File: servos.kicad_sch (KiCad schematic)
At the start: 34 parts, among them J10 Conn_01x03_Male, J18 Conn_01x03_Male, J19 Conn_01x03_Male, J5 Conn_01x03_Male, J6 Conn_01x03_Male, J7 Conn_01x03_Male, J8 Conn_01x03_Male, J9 Conn_01x03_Male, Q5 DMP2040USD, Q6 DMP2040USD, Q8 Q_NMOS_DGS, Q9 Q_NMOS_DGS

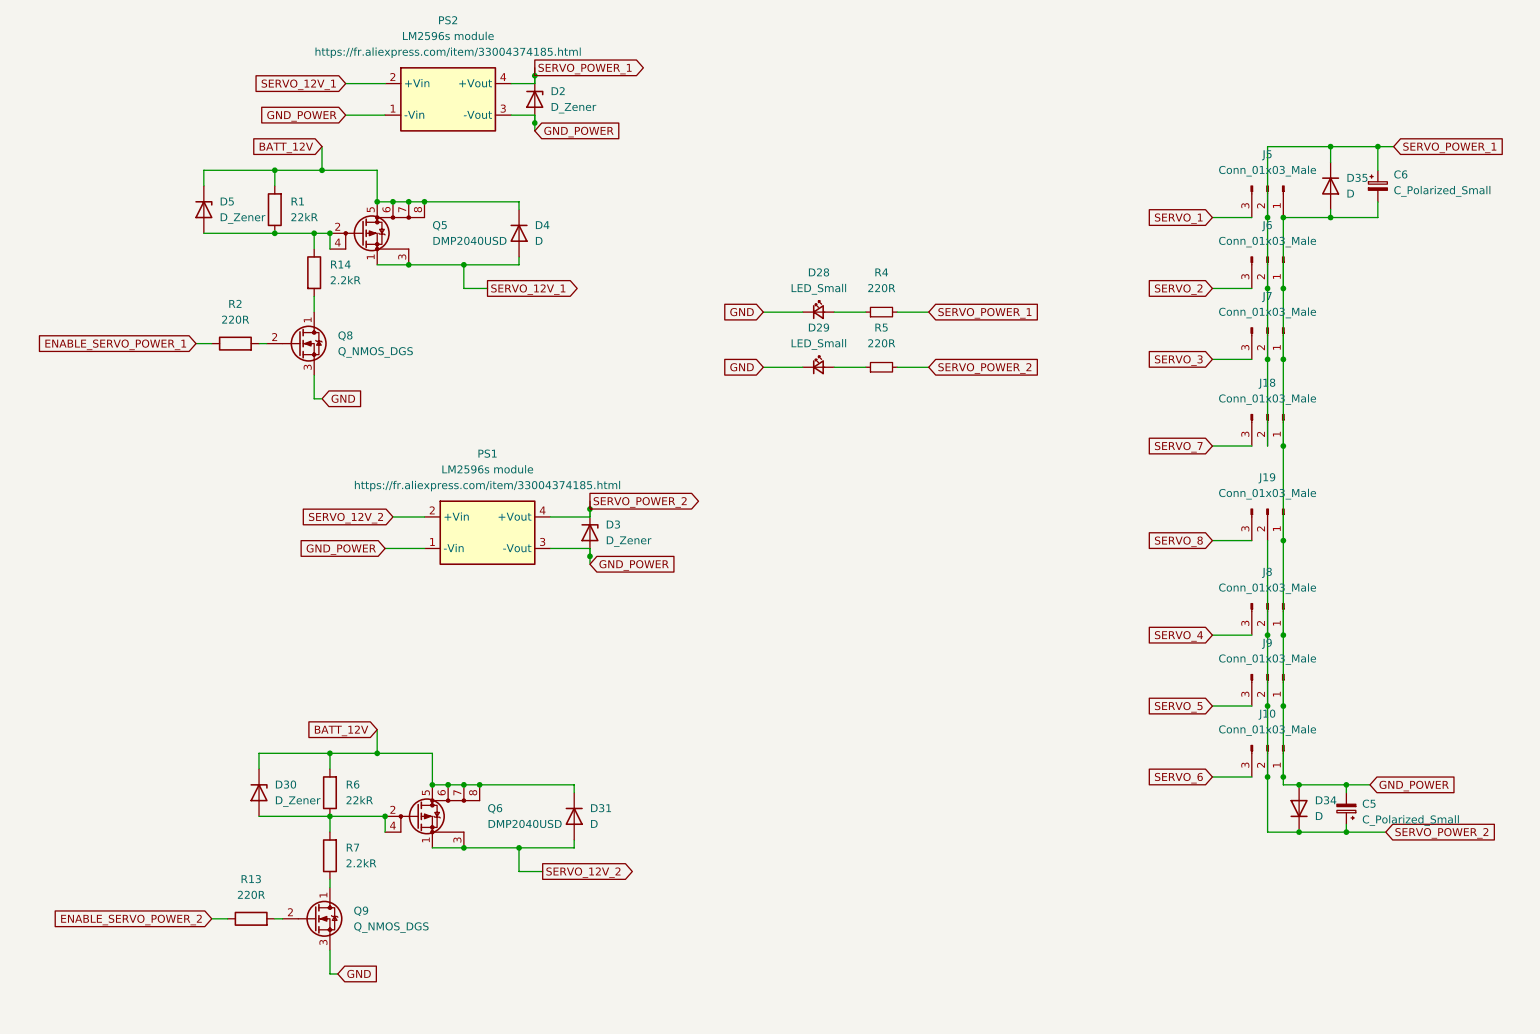
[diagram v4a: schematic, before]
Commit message: fix driving servo power (NMOS on GND) + fix 12V connector position
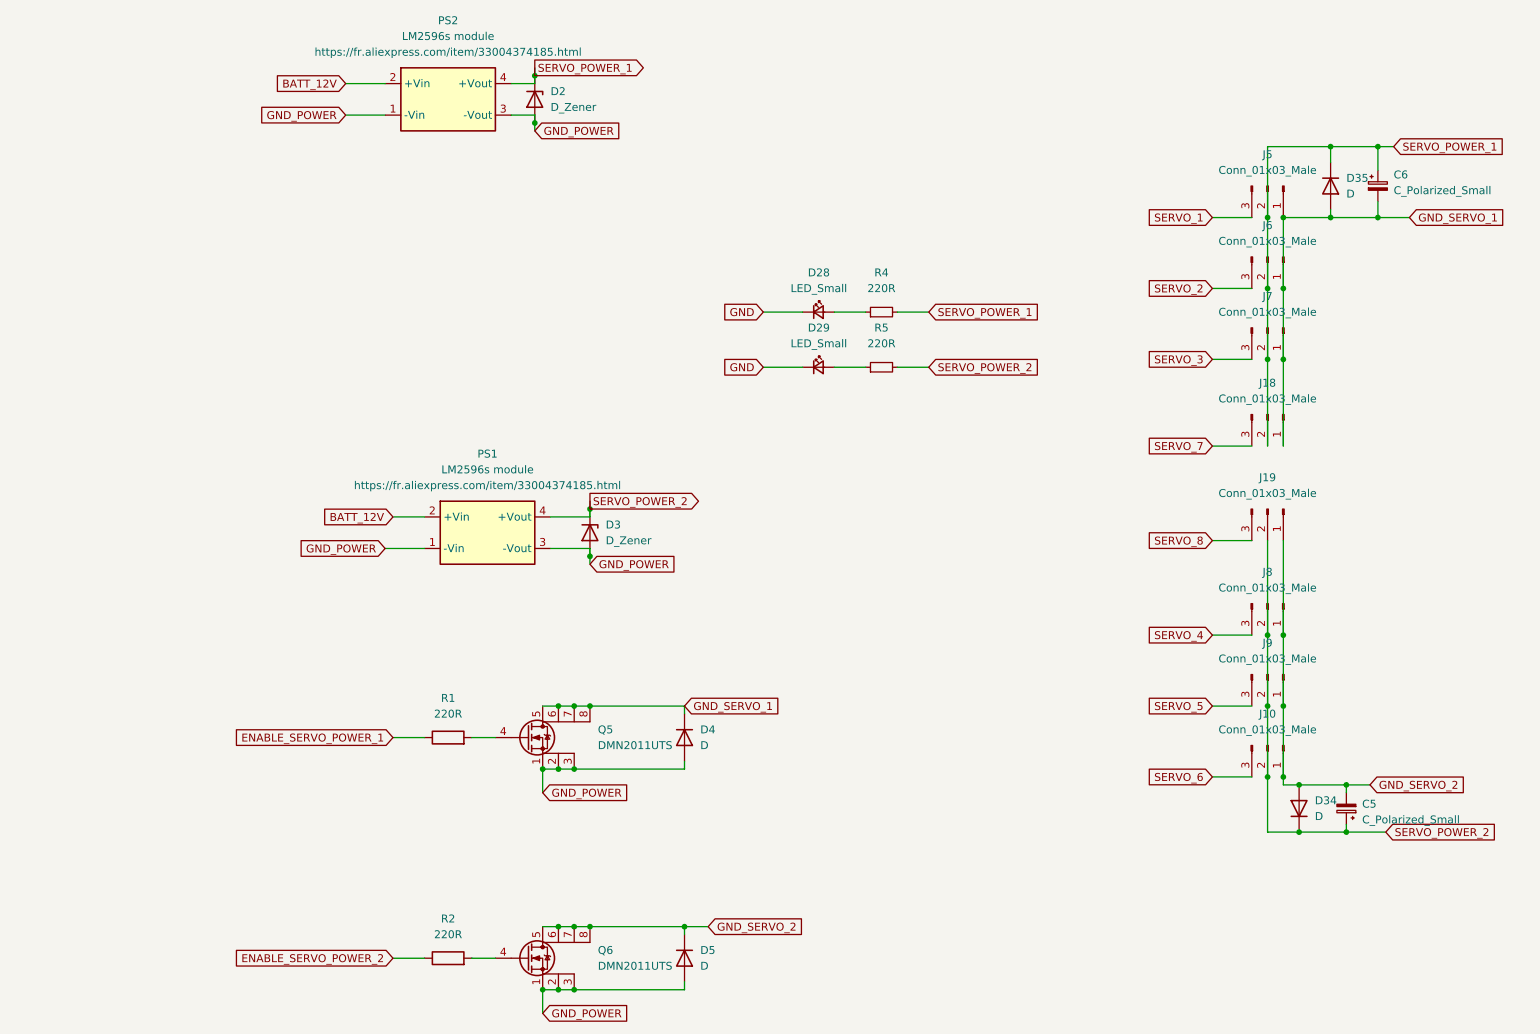
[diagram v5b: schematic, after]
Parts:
- removed D30, D5: D_Zener, Diode_SMD:D_1206_3216Metric, symbol Device:D_Zener
- removed D31: D, Diode_SMD:D_1206_3216Metric, symbol Device:D
- removed Q5, Q6: DMP2040USD, Package_SO:SO-8_3.9x4.9mm_P1.27mm, symbol New_Library_Victor:DMP2040USD
- removed Q8, Q9: Q_NMOS_DGS, symbol Device:Q_NMOS_DGS
- removed R13: 220R, Resistor_SMD:R_0603_1608Metric, symbol Device:R
- removed R14, R7: 2.2kR, Resistor_SMD:R_0603_1608Metric, symbol Device:R
- removed R6: 22kR, Resistor_SMD:R_0603_1608Metric, symbol Device:R
- added D5: D, Diode_SMD:D_1206_3216Metric, symbol Device:D
- added Q5, Q6: DMN2011UTS, Package_SO:TSSOP-8_4.4x3mm_P0.65mm, symbol New_Library_Victor:DMN2011UTS
- R1: value 22kR -> 220R
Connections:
- net SERVO_12V_2 is gone; now on net BATT_12V: PS1.2 (+Vin)
- net BATT_12V: now also PS2.2 (+Vin); no longer D4.1 (K), R1.2
- net ENABLE_SERVO_POWER_1: now also R1.1; no longer R2.1
- net ENABLE_SERVO_POWER_2: now also R2.1
- net GND_POWER: now also D4.2 (A), D5.2 (A), Q5.1 (S), Q5.2 (S), Q5.3 (S), Q6.1 (S), Q6.2 (S), Q6.3 (S); no longer C5.2, C6.2, D34.2 (A), D35.2 (A), J10.1 (Pin_1), J18.1 (Pin_1), J19.1 (Pin_1), J5.1 (Pin_1), J6.1 (Pin_1), J7.1 (Pin_1), J8.1 (Pin_1), J9.1 (Pin_1)
- net at R2.2: now also Q6.4 (G)
- removed net SERVO_12V_1: D4.2 (A), PS2.2 (+Vin)
- new net: Q5.4 (G), R1.2
- new net GND_SERVO_1: C6.2, D35.2 (A), D4.1 (K), J18.1 (Pin_1), J5.1 (Pin_1), J6.1 (Pin_1), J7.1 (Pin_1), Q5.5 (D), Q5.6 (D), Q5.7 (D), Q5.8 (D)
- new net GND_SERVO_2: C5.2, D34.2 (A), D5.1 (K), J10.1 (Pin_1), J19.1 (Pin_1), J8.1 (Pin_1), J9.1 (Pin_1), Q6.5 (D), Q6.6 (D), Q6.7 (D), Q6.8 (D)

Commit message: add AX12 connector + LED strip connector + libraries todo : add 12V connectors, change stepper connectors
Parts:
- J10, J18, J19, J5, J6, J7, J8, J9: footprint Connector_PinSocket_2.54mm:PinSocket_1x03_P2.54mm_Vertical -> Connector_PinHeader_2.54mm:PinHeader_1x03_P2.54mm_Vertical
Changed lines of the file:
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@@
     (property "Reference" "J7" (id 0) (at 210.82 69.85 90))
     (property "Value" "Conn_01x03_Male" (id 1) (at 210.82 72.39 90))
-    (property "Footprint" "Connector_PinSocket_2.54mm:PinSocket_1x03_P2.54mm_Vertical" (id 2) (at 210.82 74.93 0)
+    (property "Footprint" "Connector_PinHeader_2.54mm:PinHeader_1x03_P2.54mm_Vertical" (id 2) (at 210.82 74.93 0)
       (effects (font (size 1.27 1.27)) hide)
     )
@@
     (property "Reference" "J19" (id 0) (at 210.82 99.06 90))
     (property "Value" "Conn_01x03_Male" (id 1) (at 210.82 101.6 90))
-    (property "Footprint" "Connector_PinSocket_2.54mm:PinSocket_1x03_P2.54mm_Vertical" (id 2) (at 210.82 104.14 0)
+    (property "Footprint" "Connector_PinHeader_2.54mm:PinHeader_1x03_P2.54mm_Vertical" (id 2) (at 210.82 104.14 0)
       (effects (font (size 1.27 1.27)) hide)
     )
@@
     (property "Reference" "J5" (id 0) (at 210.82 46.99 90))
     (property "Value" "Conn_01x03_Male" (id 1) (at 210.82 49.53 90))
-    (property "Footprint" "Connector_PinSocket_2.54mm:PinSocket_1x03_P2.54mm_Vertical" (id 2) (at 210.82 52.07 0)
+    (property "Footprint" "Connector_PinHeader_2.54mm:PinHeader_1x03_P2.54mm_Vertical" (id 2) (at 210.82 52.07 0)
       (effects (font (size 1.27 1.27)) hide)
     )
@@
     (property "Reference" "J6" (id 0) (at 210.82 58.42 90))
     (property "Value" "Conn_01x03_Male" (id 1) (at 210.82 60.96 90))
-    (property "Footprint" "Connector_PinSocket_2.54mm:PinSocket_1x03_P2.54mm_Vertical" (id 2) (at 210.82 63.5 0)
+    (property "Footprint" "Connector_PinHeader_2.54mm:PinHeader_1x03_P2.54mm_Vertical" (id 2) (at 210.82 63.5 0)
       (effects (font (size 1.27 1.27)) hide)
     )
@@
     (property "Reference" "J10" (id 0) (at 210.82 137.16 90))
     (property "Value" "Conn_01x03_Male" (id 1) (at 210.82 139.7 90))
-    (property "Footprint" "Connector_PinSocket_2.54mm:PinSocket_1x03_P2.54mm_Vertical" (id 2) (at 210.82 142.24 0)
+    (property "Footprint" "Connector_PinHeader_2.54mm:PinHeader_1x03_P2.54mm_Vertical" (id 2) (at 210.82 142.24 0)
       (effects (font (size 1.27 1.27)) hide)
     )
@@
     (property "Reference" "J18" (id 0) (at 210.82 83.82 90))
     (property "Value" "Conn_01x03_Male" (id 1) (at 210.82 86.36 90))
-    (property "Footprint" "Connector_PinSocket_2.54mm:PinSocket_1x03_P2.54mm_Vertical" (id 2) (at 210.82 88.9 0)
+    (property "Footprint" "Connector_PinHeader_2.54mm:PinHeader_1x03_P2.54mm_Vertical" (id 2) (at 210.82 88.9 0)
       (effects (font (size 1.27 1.27)) hide)
     )
@@
     (property "Reference" "J9" (id 0) (at 210.82 125.73 90))
     (property "Value" "Conn_01x03_Male" (id 1) (at 210.82 128.27 90))
-    (property "Footprint" "Connector_PinSocket_2.54mm:PinSocket_1x03_P2.54mm_Vertical" (id 2) (at 210.82 130.81 0)
+    (property "Footprint" "Connector_PinHeader_2.54mm:PinHeader_1x03_P2.54mm_Vertical" (id 2) (at 210.82 130.81 0)
       (effects (font (size 1.27 1.27)) hide)
     )
@@
     (property "Reference" "J8" (id 0) (at 210.82 114.3 90))
     (property "Value" "Conn_01x03_Male" (id 1) (at 210.82 116.84 90))
-    (property "Footprint" "Connector_PinSocket_2.54mm:PinSocket_1x03_P2.54mm_Vertical" (id 2) (at 210.82 119.38 0)
-      (effects (font (size 1.27 1.27)) hide)
-    )
+    (property "Footprint" "Connector_PinHeader_2.54mm:PinHeader_1x03_P2.54mm_Vertical" (id 2) (at 210.82 119.38 0)
+      (effects (font (size 1.27 1.27)) hide)
+    )

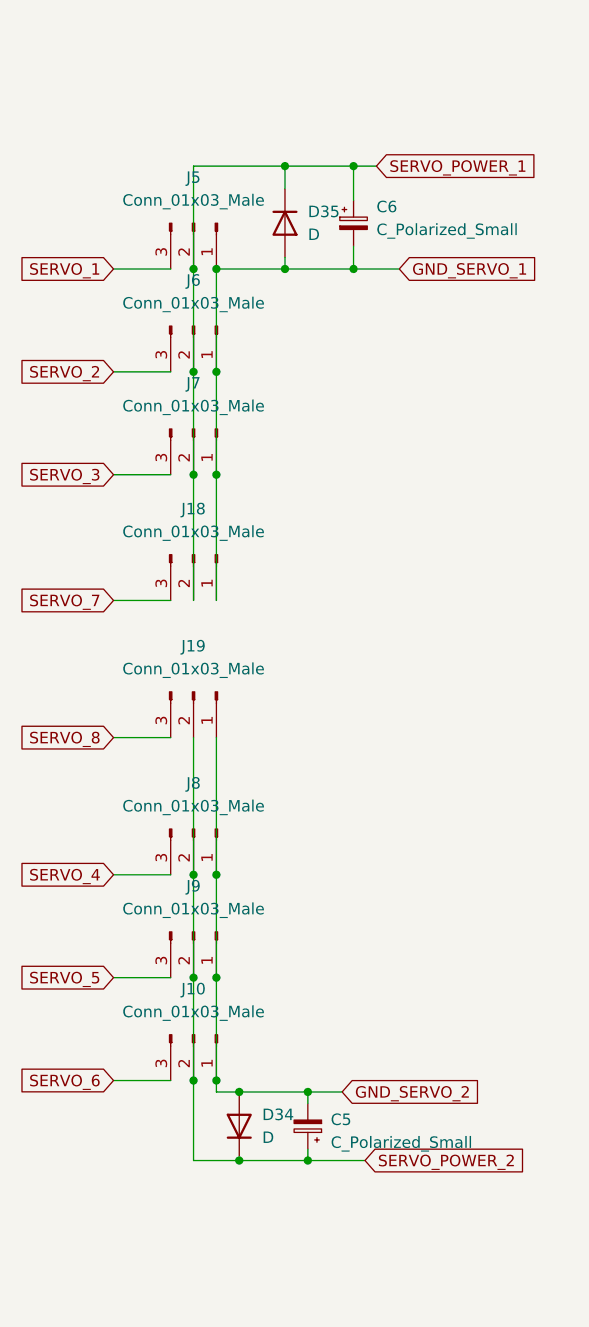
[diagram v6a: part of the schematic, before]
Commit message: add second AX12 connector + change stepper connectors + add 12V connector. Todo : add SPI for RFID
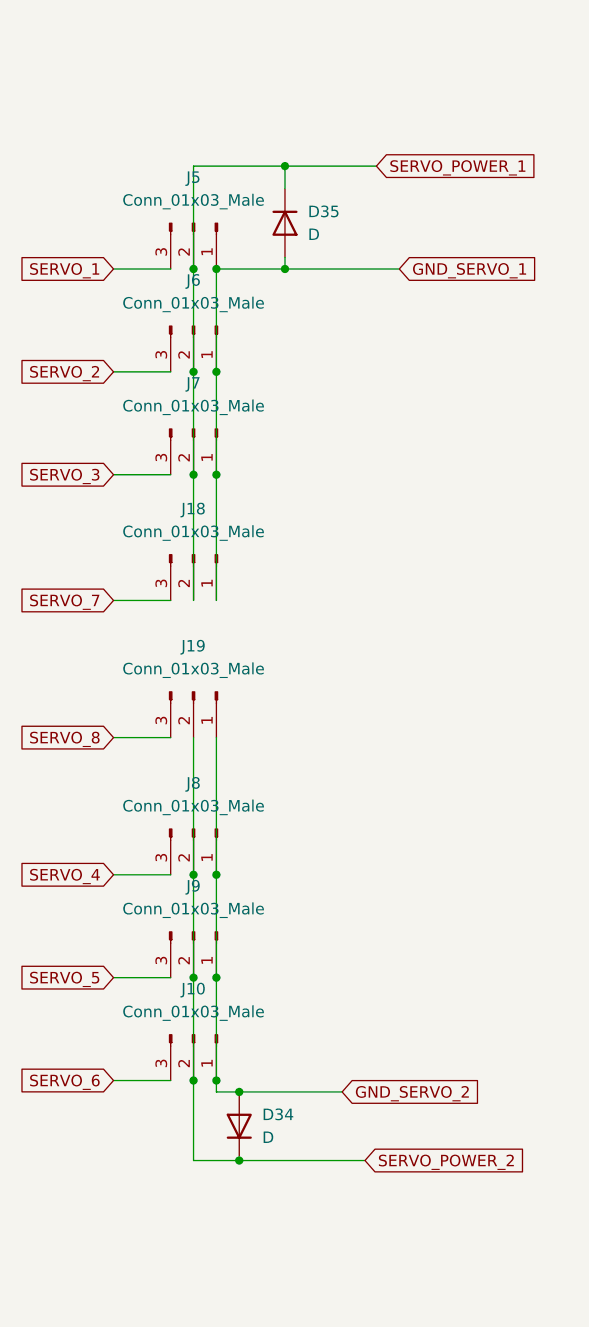
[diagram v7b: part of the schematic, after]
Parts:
- removed C5, C6: C_Polarized_Small, Capacitor_THT:CP_Radial_D8.0mm_P2.50mm, symbol Device:C_Polarized_Small
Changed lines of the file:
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@@
   (junction (at 220.98 57.15) (diameter 0) (color 0 0 0 0)
   )
-  (junction (at 223.52 148.59) (diameter 0) (color 0 0 0 0)
-  )
   (junction (at 210.82 80.01) (diameter 0) (color 0 0 0 0)
   )
-  (junction (at 228.6 45.72) (diameter 0) (color 0 0 0 0)
-  )
   (junction (at 210.82 57.15) (diameter 0) (color 0 0 0 0)
   )
@@
   (junction (at 215.9 148.59) (diameter 0) (color 0 0 0 0)
   )
-  (junction (at 223.52 156.21) (diameter 0) (color 0 0 0 0)
-  )
   (junction (at 213.36 57.15) (diameter 0) (color 0 0 0 0)
   )
   (junction (at 101.6 135.89) (diameter 0) (color 0 0 0 0)
   )
-  (junction (at 228.6 57.15) (diameter 0) (color 0 0 0 0)
-  )
   (junction (at 96.52 181.61) (diameter 0) (color 0 0 0 0)
   )
@@
     (stroke (width 0) (type default) (color 0 0 0 0))
   )
-  (wire (pts (xy 228.6 49.53) (xy 228.6 45.72))
-    (stroke (width 0) (type default) (color 0 0 0 0))
-  )
   (wire (pts (xy 140.97 81.28) (xy 146.05 81.28))
     (stroke (width 0) (type default) (color 0 0 0 0))
@@
     (stroke (width 0) (type default) (color 0 0 0 0))
   )
-  (wire (pts (xy 228.6 45.72) (xy 231.14 45.72))
-    (stroke (width 0) (type default) (color 0 0 0 0))
-  )
   (wire (pts (xy 95.25 110.49) (xy 101.6 110.49))
     (stroke (width 0) (type default) (color 0 0 0 0))
@@
     (stroke (width 0) (type default) (color 0 0 0 0))
   )
-  (wire (pts (xy 228.6 57.15) (xy 233.68 57.15))
-    (stroke (width 0) (type default) (color 0 0 0 0))
-  )
   (wire (pts (xy 213.36 124.46) (xy 213.36 135.89))
     (stroke (width 0) (type default) (color 0 0 0 0))
@@
     (stroke (width 0) (type default) (color 0 0 0 0))
   )
-  (wire (pts (xy 229.87 156.21) (xy 223.52 156.21))
-    (stroke (width 0) (type default) (color 0 0 0 0))
-  )
-  (wire (pts (xy 220.98 45.72) (xy 228.6 45.72))
+  (wire (pts (xy 220.98 45.72) (xy 231.14 45.72))
     (stroke (width 0) (type default) (color 0 0 0 0))
   )
@@
     (stroke (width 0) (type default) (color 0 0 0 0))
   )
-  (wire (pts (xy 228.6 57.15) (xy 220.98 57.15))
+  (wire (pts (xy 220.98 57.15) (xy 233.68 57.15))
     (stroke (width 0) (type default) (color 0 0 0 0))
   )
@@
     (stroke (width 0) (type default) (color 0 0 0 0))
   )
-  (wire (pts (xy 228.6 54.61) (xy 228.6 57.15))
-    (stroke (width 0) (type default) (color 0 0 0 0))
-  )
   (wire (pts (xy 213.36 147.32) (xy 213.36 148.59))
     (stroke (width 0) (type default) (color 0 0 0 0))
   )
-  (wire (pts (xy 223.52 154.94) (xy 223.52 156.21))
-    (stroke (width 0) (type default) (color 0 0 0 0))
-  )
   (wire (pts (xy 210.82 156.21) (xy 215.9 156.21))
     (stroke (width 0) (type default) (color 0 0 0 0))
@@
     (stroke (width 0) (type default) (color 0 0 0 0))
   )
-  (wire (pts (xy 223.52 148.59) (xy 223.52 149.86))
-    (stroke (width 0) (type default) (color 0 0 0 0))
-  )
   (wire (pts (xy 213.36 148.59) (xy 215.9 148.59))
     (stroke (width 0) (type default) (color 0 0 0 0))
@@
     (stroke (width 0) (type default) (color 0 0 0 0))
   )
-  (wire (pts (xy 223.52 148.59) (xy 227.33 148.59))
+  (wire (pts (xy 215.9 148.59) (xy 227.33 148.59))
     (stroke (width 0) (type default) (color 0 0 0 0))
   )
@@
     (stroke (width 0) (type default) (color 0 0 0 0))
   )
-  (wire (pts (xy 215.9 148.59) (xy 223.52 148.59))
-    (stroke (width 0) (type default) (color 0 0 0 0))
-  )
   (wire (pts (xy 140.97 72.39) (xy 146.05 72.39))
     (stroke (width 0) (type default) (color 0 0 0 0))
@@
     (stroke (width 0) (type default) (color 0 0 0 0))
   )
-  (wire (pts (xy 223.52 156.21) (xy 215.9 156.21))
+  (wire (pts (xy 215.9 156.21) (xy 229.87 156.21))
     (stroke (width 0) (type default) (color 0 0 0 0))
   )
@@
     (pin "3")
   )
-  (symbol (lib_id "Device:C_Polarized_Small") (at 223.52 152.4 180) (unit 1)
-    (in_bom yes) (on_board yes) (fields_autoplaced)
-    (property "Reference" "C5" (id 0) (at 226.06 151.676 0)
-      (effects (font (size 1.27 1.27)) (justify right))
-    )
-    (property "Value" "C_Polarized_Small" (id 1) (at 226.06 154.216 0)
-      (effects (font (size 1.27 1.27)) (justify right))
-    )
-    (property "Footprint" "Capacitor_THT:CP_Radial_D8.0mm_P2.50mm" (id 2) (at 223.52 152.4 0)
-      (effects (font (size 1.27 1.27)) hide)
-    )
-    (property "Datasheet" "~" (id 3) (at 223.52 152.4 0)
-      (effects (font (size 1.27 1.27)) hide)
-    )
-    (pin "1")
-    (pin "2")
-  )
   (symbol (lib_id "Device:D") (at 116.84 140.97 270) (unit 1)
     (in_bom yes) (on_board yes) (fields_autoplaced)
@@
     (pin "3")
   )
-  (symbol (lib_id "Device:C_Polarized_Small") (at 228.6 52.07 0) (unit 1)
-    (in_bom yes) (on_board yes) (fields_autoplaced)
-    (property "Reference" "C6" (id 0) (at 231.14 50.2538 0)
-      (effects (font (size 1.27 1.27)) (justify left))
-    )
-    (property "Value" "C_Polarized_Small" (id 1) (at 231.14 52.7938 0)
-      (effects (font (size 1.27 1.27)) (justify left))
-    )
-    (property "Footprint" "Capacitor_THT:CP_Radial_D8.0mm_P2.50mm" (id 2) (at 228.6 52.07 0)
-      (effects (font (size 1.27 1.27)) hide)
-    )
-    (property "Datasheet" "~" (id 3) (at 228.6 52.07 0)
-      (effects (font (size 1.27 1.27)) hide)
-    )
-    (pin "1")
-    (pin "2")
-  )
   (symbol (lib_id "Device:D_Zener") (at 92.71 38.1 270) (unit 1)
